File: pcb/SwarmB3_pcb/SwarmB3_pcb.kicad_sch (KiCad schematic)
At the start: 53 parts, among them J1 5v_3Pi, J10 ItsyBitsyRight, J11 ItsyBitsyLeft, J12 ItsyBitsyBottom, J2 GND_3Pi, J3 I2C_3V3_Exp, J4 Conn_02x15_M5Stack_Core2, J5 I2C_3Pi, J6 3PI_SWTCH, J8 ProxA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

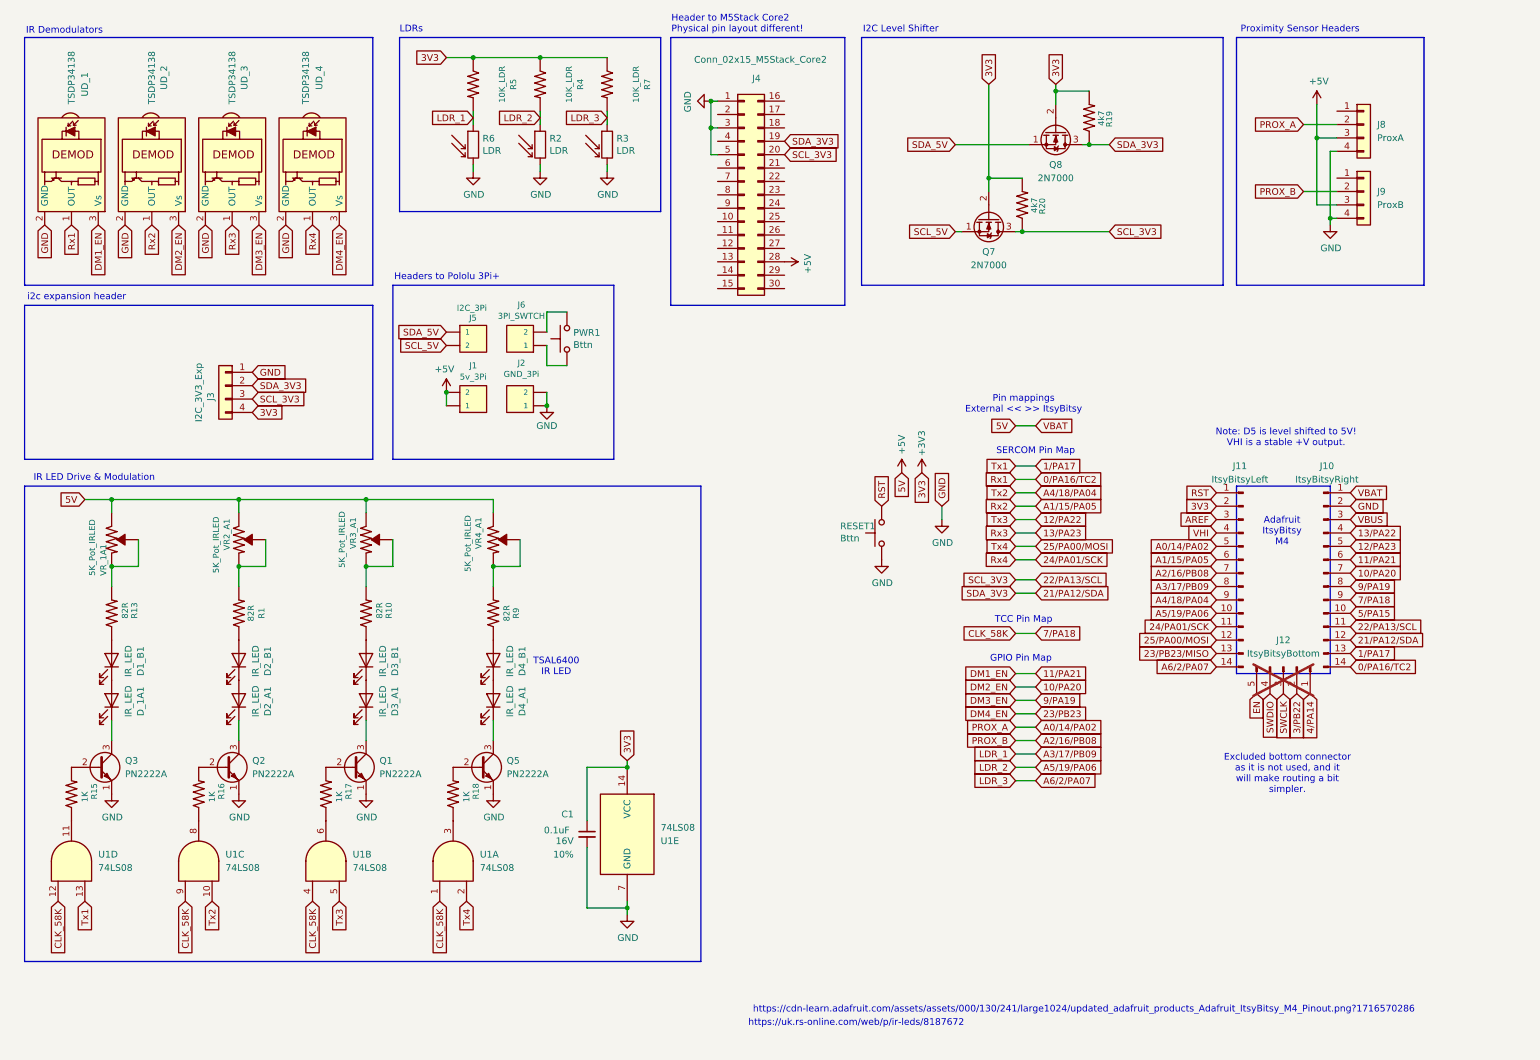
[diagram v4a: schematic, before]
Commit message: Lots and lots of debugging between hardware and software.  The pcb design worked on the assumption that the UART tx could be inverted in software, as stated in the SAMD51 datasheet.  However, it doesn't work as I expected.  It seems to invert the data, but the idle state remains high.  This causes issues for IR communication because I don't want to saturate the environment with the carrier wave whilst communication is not occuring. I tried a software fix, pulling the gpio low between transmissions.  However, I can't seem to restore the GPIO properly without messing up the protocol overall. I got as far as seeing the bit pattern shifted by 1 bit, which is occuring because the receiver is mis-registering the start bit.  When I look at both sides of the communication on the oscilloscope, I can see that for a batch send (like 10 bytes), the first byte is dropping the start bit.  I haven't been able to get to the bottom of why.  If I do not invert the tx, the problem goes away, but I don't want a non-inverted signal (saturation problem).  I tried some other logic gates.  Surprisingly, 74hc32 (OR) works as a drop in - however, it does mean that for data logic 1, the data stream is actually an on/off pulse train - which is not ideal.  The receiver seems quite robust to this, the datasheet has measures for this sort of thing.  However, I don't want a board that could cause communication defects alongside from what I am investigating in research.  A possible fix is to implement active low LED drivers, which would necessitate an extra transister per UART (e.g. +4).  I don't fancy soldering that, so instead I've updated the pcb to pass tx outputs through a 74hc14 first.  I've tested this on breadboard and it works fine.  It means I can just use the UART interfaces normally without any software SAMD51 inversion.  The current code (ItsyBitsy_test) is a mess from all my debugging chopping and changes.  I'll refactor after testing the new pcb when it arrives.
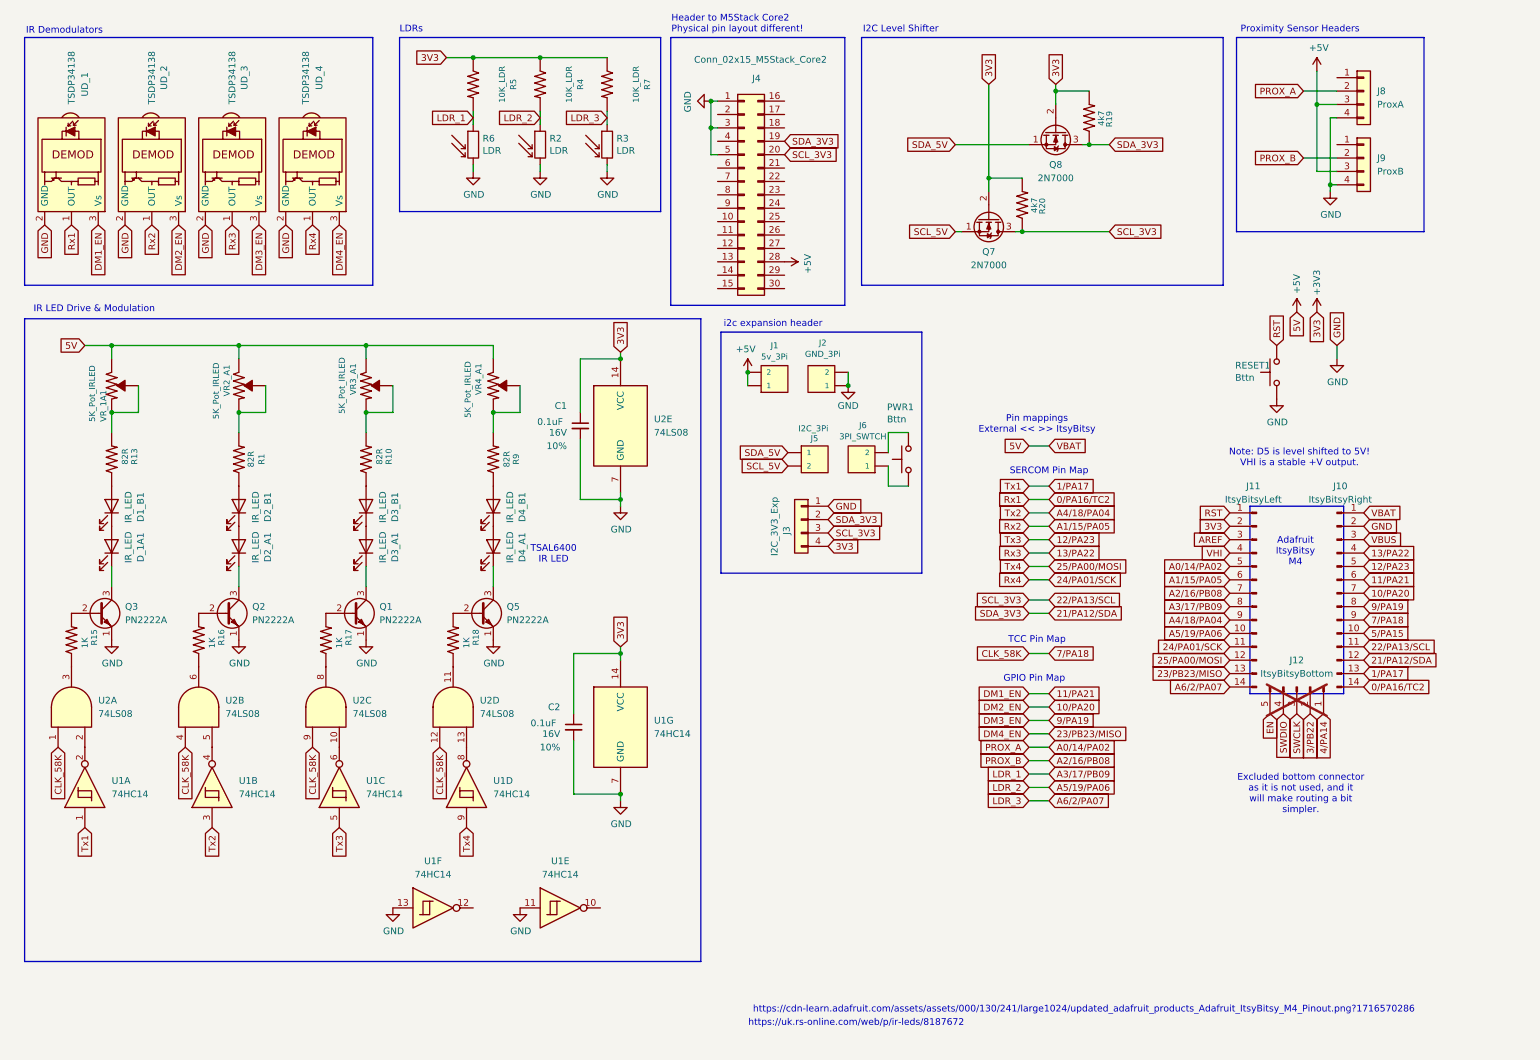
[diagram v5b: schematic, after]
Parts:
- removed U1: 74LS08, Package_DIP:DIP-14_W7.62mm_Socket, symbol 74xx:74LS08
- added C2: 0.1uF, Capacitor_THT:C_Disc_D4.7mm_W2.5mm_P5.00mm, symbol PCM_SparkFun-Capacitor:0.1uF_0402_16V_10%
- added U1: 74HC14, Package_DIP:DIP-14_W7.62mm_Socket, symbol 74xx:74HC14
- added U2: 74LS08, Package_DIP:DIP-14_W7.62mm_Socket, symbol 74xx:74LS08
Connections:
- net 13/PA23 is gone; now on net 13/PA22: UD_3.1 (OUT)
- net 23/PB23 is gone; now on net 23/PB23/MISO: UD_4.3 (Vs)
- net +3V3: now also C2.1, U1.14 (VCC), U2.14 (VCC)
- net 12/PA23: now also U1.5
- net 1/PA17: now also U1.1
- net 25/PA00/MOSI: now also U1.9
- net 7/PA18: now also U2.1, U2.12, U2.4, U2.9
- net A4/18/PA04: now also U1.3
- net GND: now also C2.2, U1.11, U1.13, U1.7 (GND), U2.7 (GND)
- net at R16.1: now also U2.6
- net at R15.1: now also U2.3
- net at R18.1: now also U2.11
- net at R17.1: now also U2.8
- new net: U1.8, U2.13
- new net: U1.2, U2.2
- new net: U1.4, U2.5
- new net: U1.6, U2.10
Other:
- note removed: "Headers to Pololu 3Pi+"
- moved on the sheet: C1, D1_B1, D2_A1, D2_B1, D3_A1, D3_B1, D4_A1, D4_B1, D_1A1, J1, J10, J11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
